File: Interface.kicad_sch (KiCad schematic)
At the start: 46 parts, among them J6301 PV, J6302 PV, J6303 VBUS, J6304 PV, J6305 PV, J6306 PV, J6307 PV, J6308 Chan, J6309 Chan, J6310 Chan, J6311 Chan, J6312 Chan, J6313 Chan, J6314 Chan, J6315 Chan, J6316 Chan_BUS, J6317 Chan_BUS, J6318 VBUS, J6319 VBUS, J6320 Battery, J6321 Battery, J6322 HEADER_PV, J6323 HEADER_PV, J6324 HEADER_CHAN, J6325 HEADER_CHAN, J6326 HEADER_CHAN, J6327 HEADER_CHAN, J6328 VBUS, J6329 SPI, J6330 UART, J6331 BATT_PACK, J801 BATT_PACK

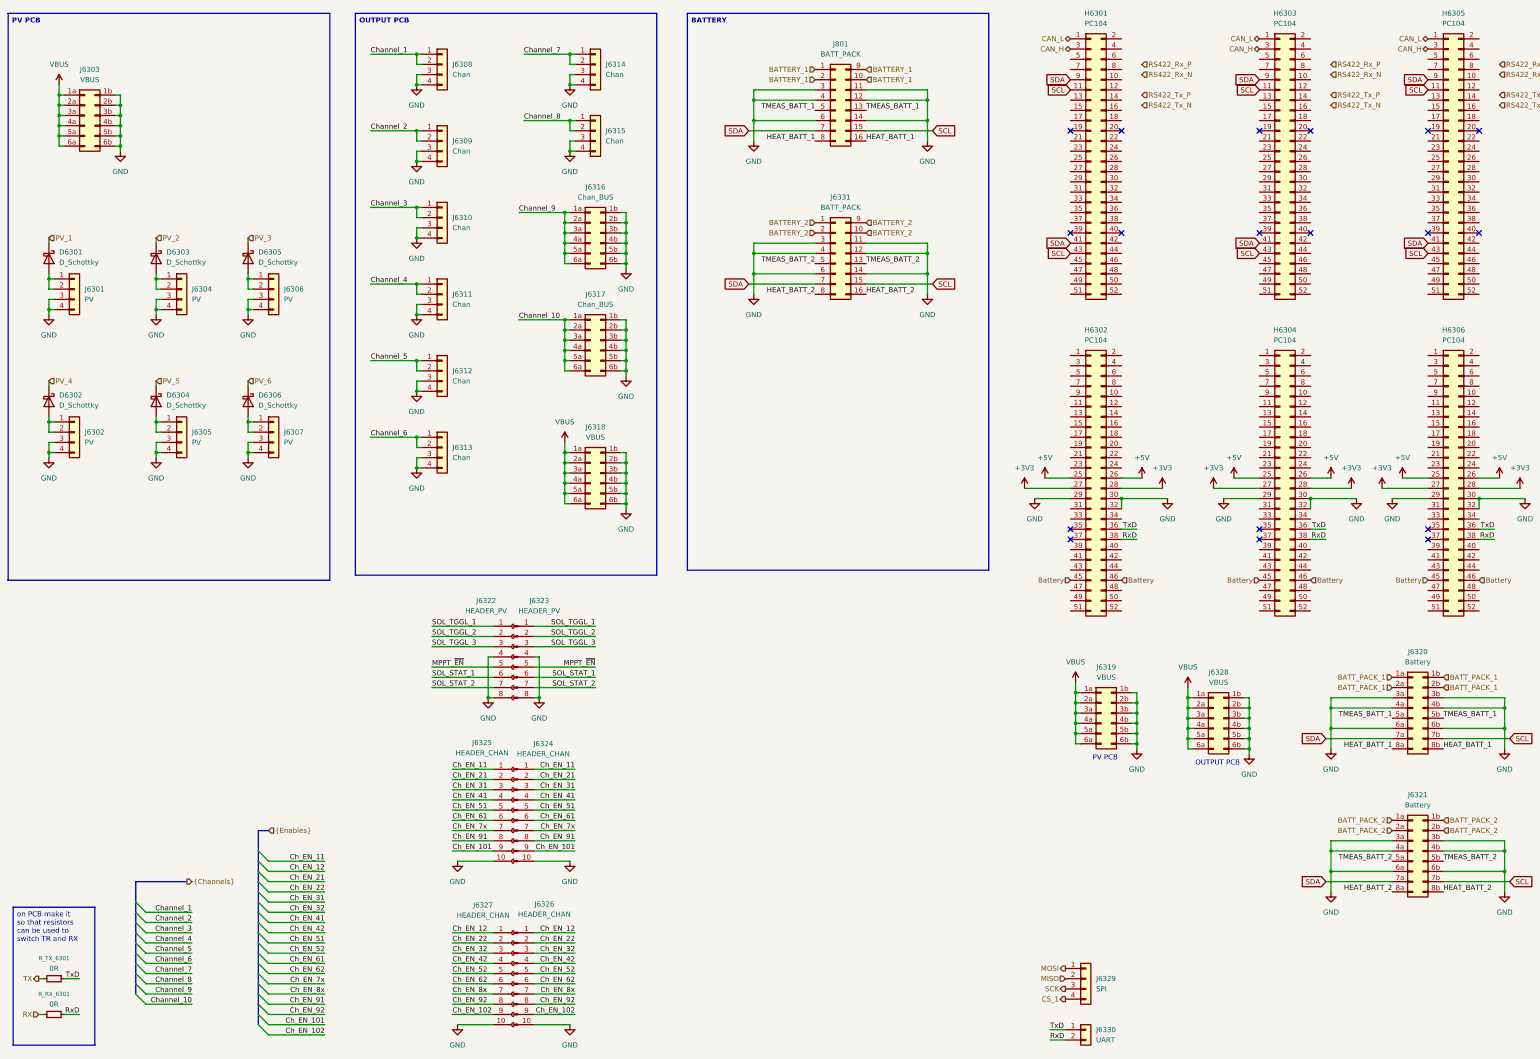
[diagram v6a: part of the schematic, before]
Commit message: reduced number of DCDC converter for PV panels; updated test pcb
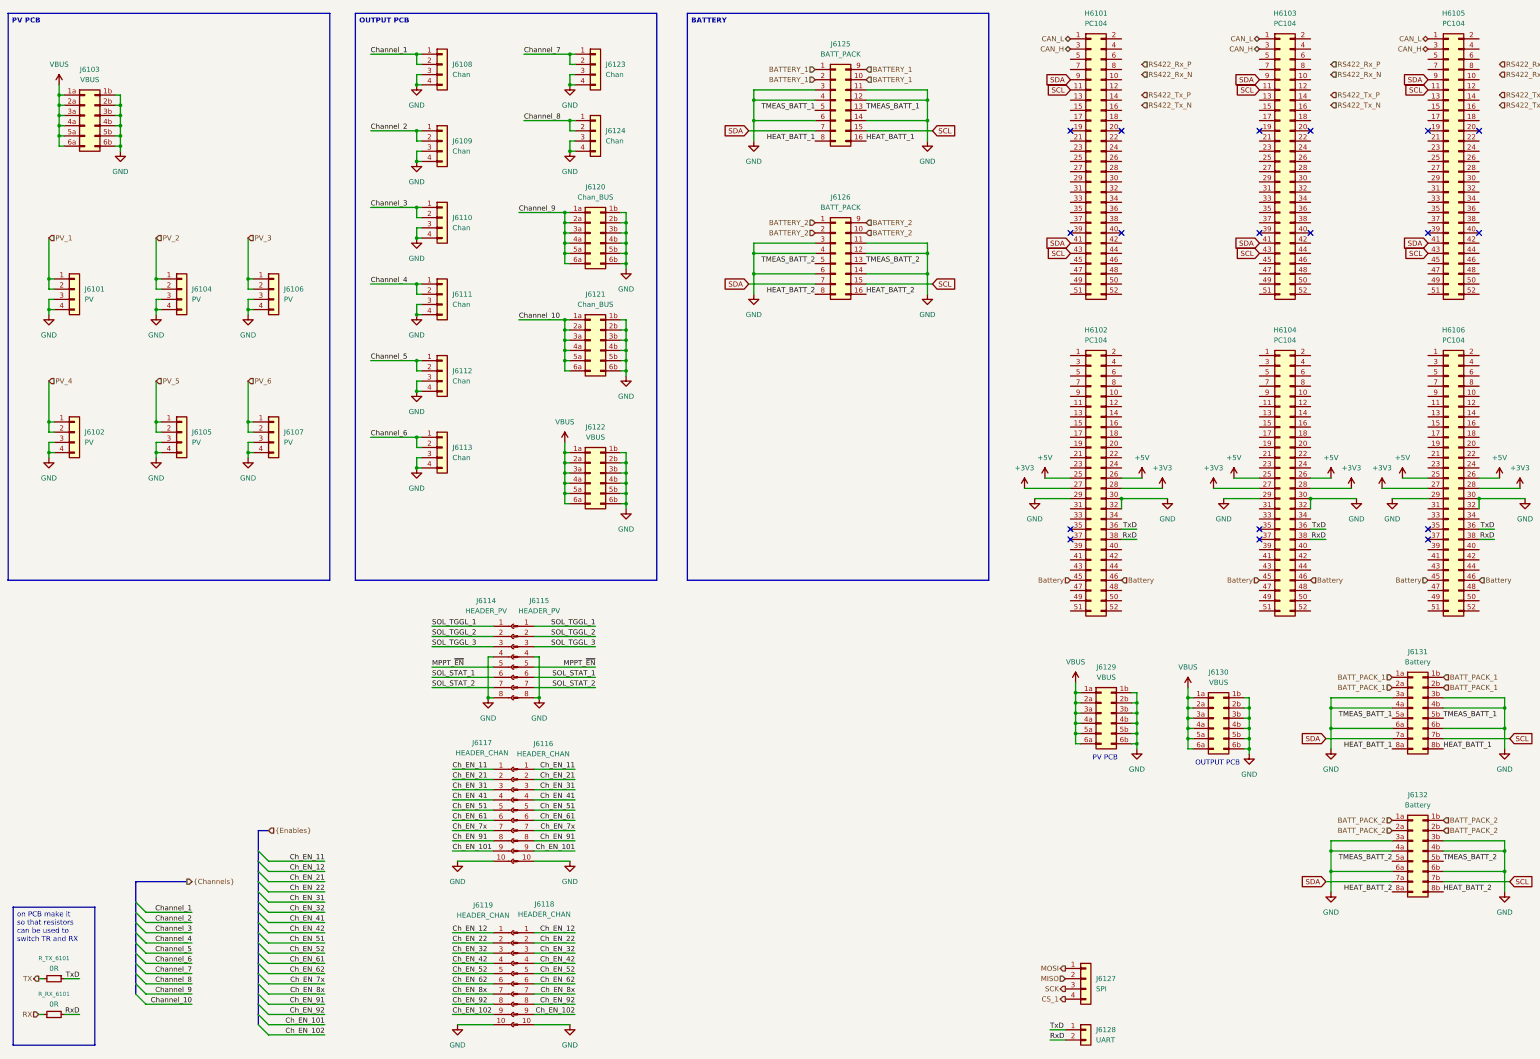
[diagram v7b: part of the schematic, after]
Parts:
- removed D6301, D6302, D6303, D6304, D6305, D6306: D_Schottky, Diode_SMD:D_0805_2012Metric, symbol Device:D_Schottky
- renumbered H6301 to H6101, H6302 to H6102, H6303 to H6103, H6304 to H6104, H6305 to H6105, H6306 to H6106, J6301 to J6101, J6302 to J6102, J6303 to J6103, J6304 to J6104, J6305 to J6105, J6306 to J6106, J6307 to J6107, J6308 to J6108, J6309 to J6109, J6310 to J6110, J6311 to J6111, J6312 to J6112, J6313 to J6113, J6322 to J6114, J6323 to J6115, J6324 to J6116, J6325 to J6117, J6326 to J6118, J6327 to J6119, J6316 to J6120, J6317 to J6121, J6318 to J6122, J6314 to J6123, J6315 to J6124, J801 to J6125, J6331 to J6126, J6329 to J6127, J6330 to J6128, J6319 to J6129, J6328 to J6130, J6320 to J6131, J6321 to J6132, R_RX_6301 to R_RX_6101, R_TX_6301 to R_TX_6101
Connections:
- net PV_1: now also J6101.1 (Pin_1), J6101.2 (Pin_2)
- net PV_2: now also J6104.1 (Pin_1), J6104.2 (Pin_2)
- net PV_3: now also J6106.1 (Pin_1), J6106.2 (Pin_2)
- net PV_4: now also J6102.1 (Pin_1), J6102.2 (Pin_2)
- net PV_5: now also J6105.1 (Pin_1), J6105.2 (Pin_2)
- net PV_6: now also J6107.1 (Pin_1), J6107.2 (Pin_2)

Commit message: added missing heater connectors
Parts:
- added J5901, J5902, J5903, J5904: HEATER, Connector_Molex:Molex_CLIK-Mate_502494-0470_1x04-1MP_P2.00mm_Horizontal, symbol Connector_Generic:Conn_01x04
- R_RX_6101, R_TX_6101: value 0R -> 0
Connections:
- net GND: now also J5901.3 (Pin_3), J5901.4 (Pin_4), J5902.3 (Pin_3), J5902.4 (Pin_4), J5903.3 (Pin_3), J5903.4 (Pin_4), J5904.3 (Pin_3), J5904.4 (Pin_4)
- new net HEATER_1: J5901.1 (Pin_1), J5901.2 (Pin_2), J5902.1 (Pin_1), J5902.2 (Pin_2)
- new net HEATER_2: J5903.1 (Pin_1), J5903.2 (Pin_2), J5904.1 (Pin_1), J5904.2 (Pin_2)
